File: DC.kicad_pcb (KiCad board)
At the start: 4 copper layers, 125 x 125 mm, 38 parts, among them U6 MCP2551-I-P, U7 NUCLEO-F302R8

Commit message: Imported footprints
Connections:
- U6 pad 8: GND -> Net-(U6-Rs)
- U7 pad CN10_1: unconnected-(U7B-PC9-PadCN10_1) -> /I2C1_SDA
- U7 pad CN10_22: /SupBattMonitor -> unconnected-(U7B-PB2-PadCN10_22)
- U7 pad CN10_23: /AccelIn -> unconnected-(U7B-PA8-PadCN10_23)
- U7 pad CN10_3: unconnected-(U7B-PB8-PadCN10_3) -> /I2C1_CLK
- U7 pad CN7_28: unconnected-(U7A-PA0-PadCN7_28) -> /AccelIn

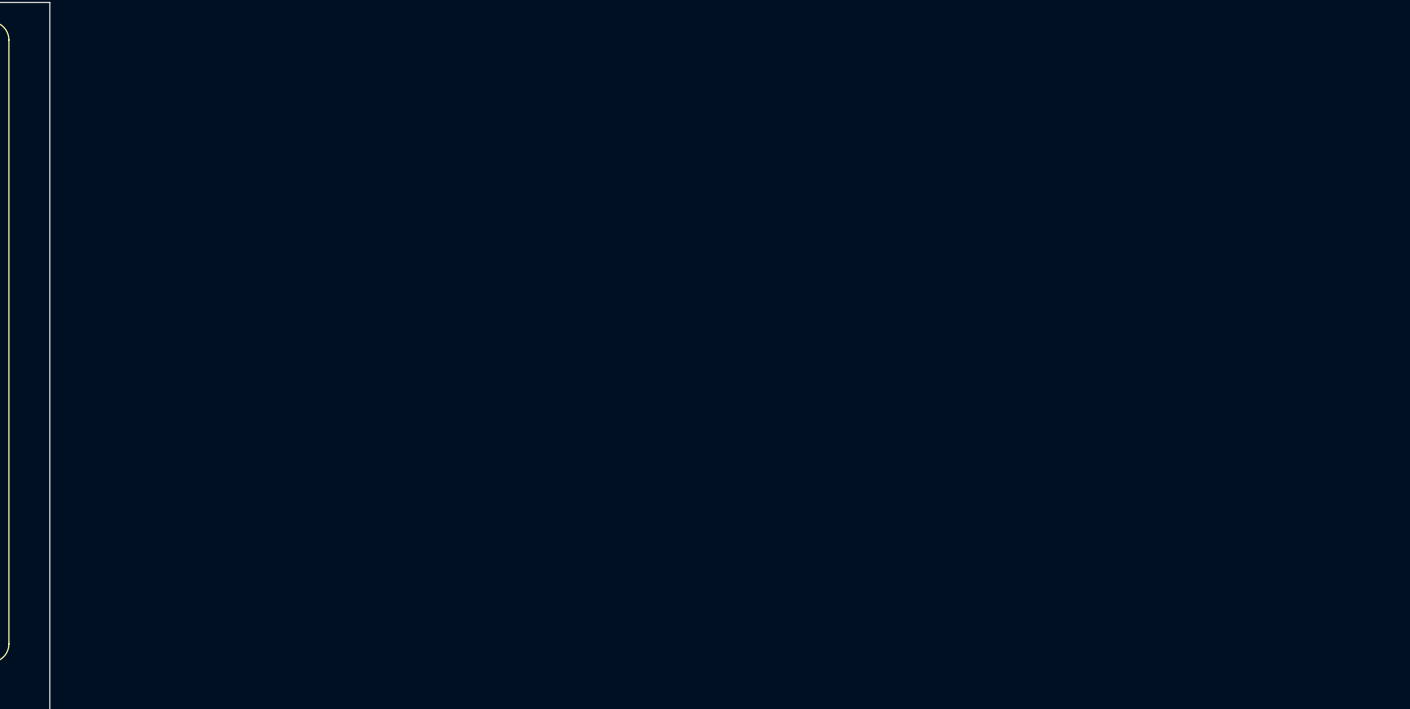
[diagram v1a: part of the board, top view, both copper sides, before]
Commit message: Added LCD!
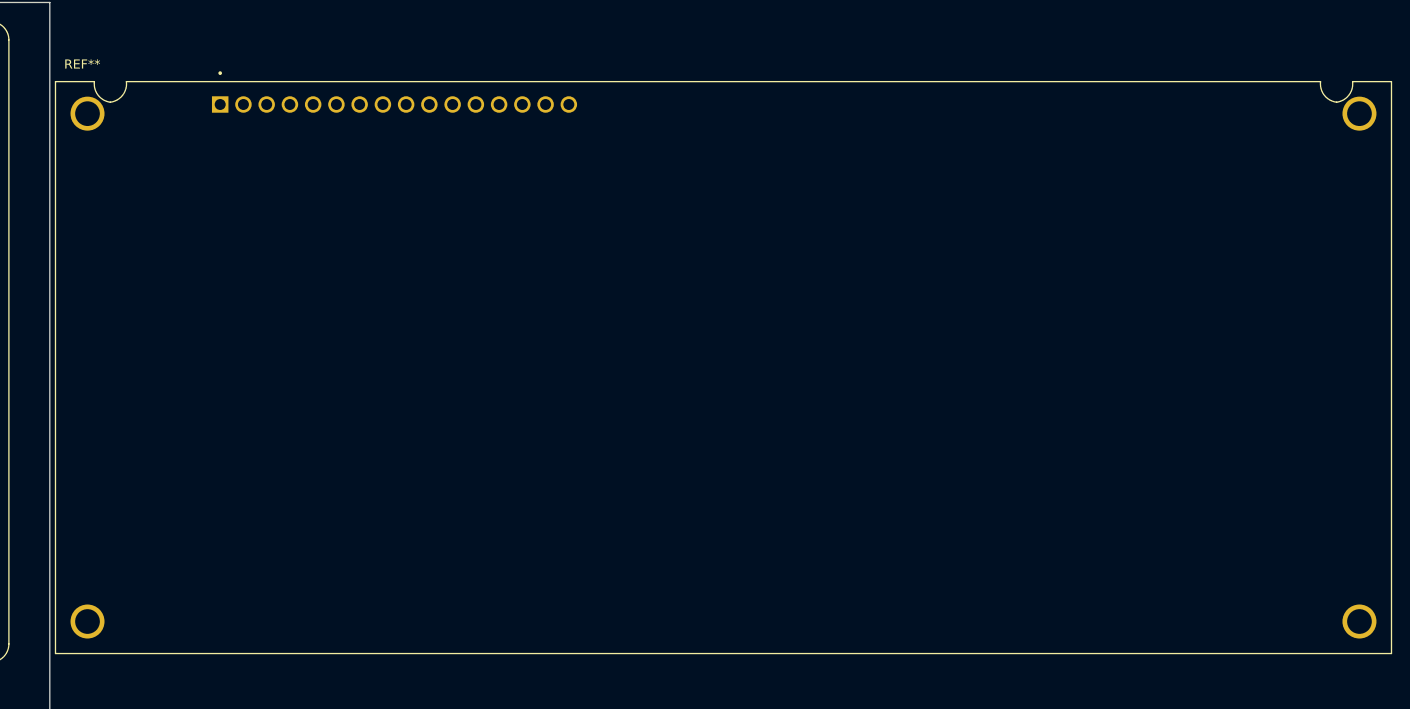
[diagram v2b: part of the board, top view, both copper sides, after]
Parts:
- added REF**: LCD_NHD-0420E2Z-FSW-GBW, MiscellaneousLibrary:LCD_NHD-0420E2Z-FSW-GBW, F.Cu at (256.5, 79.0)

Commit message: Symbols all have a footprint and LCD added
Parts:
- removed REF**: LCD_NHD-0420E2Z-FSW-GBW, MiscellaneousLibrary:LCD_NHD-0420E2Z-FSW-GBW
- added C10: CL31B225KBHNNNE, Capacitor_SMD:CAPC3216X180N, F.Cu at (159.5, 38.5)
- added C11: CL31B105KAHNNNE, Capacitor_SMD:CAPC3216X180N, F.Cu at (167.0, 86.5)
- added C12: C3216X7R2A474K160AA, Capacitor_SMD:CAPC3216X180N, F.Cu at (172.5, 86.5)
- added C8: CL31B225KBHNNNE, Capacitor_SMD:CAPC3216X180N, F.Cu at (161.5, 103.5)
- added C9: CL31B225KBHNNNE, Capacitor_SMD:CAPC3216X180N, F.Cu at (131.5, 103.5)
- added D1: LTST-C190KSKT, LED_SMD:LEDM1608X80, F.Cu at (144.1, 247.6)
- added D2: LTST-C193TBKT-5A, Fuse:Fuse_0603_1608Metric, F.Cu at (138.7, 192.1)
- added D4: LTST-C193TBKT-5A, Fuse:Fuse_0603_1608Metric, F.Cu at (138.7, 194.6)
- added D5: LTST-C193TBKT-5A, Fuse:Fuse_0603_1608Metric, F.Cu at (138.7, 197.1)
- added D6: LTST-C193TBKT-5A, Fuse:Fuse_0603_1608Metric, F.Cu at (138.7, 199.6)
- added D7: LTST-C193TBKT-5A, Fuse:Fuse_0603_1608Metric, F.Cu at (138.7, 202.1)
- added DS1: NHD-C0220BIZ-FSW-FBW-3V3M, Display:LCD_NHD-C0220BIZ-FSW-FBW-3V3M, F.Cu at (174.5, 62.6)
- added F10: 0466.125NR, Fuse:FUSC3215X66N, F.Cu at (133.5, 186.1)
- added F11: 0466.125NR, Fuse:FUSC3215X66N, F.Cu at (138.6, 178.1)
- added F12: 0466.125NR, Fuse:FUSC3215X66N, F.Cu at (138.6, 180.8)
- added F13: 0466.125NR, Fuse:FUSC3215X66N, F.Cu at (138.6, 183.5)
- added F14: 0466.125NR, Fuse:FUSC3215X66N, F.Cu at (138.6, 186.1)
- added F15: 0466.125NR, Fuse:FUSC3215X66N, F.Cu at (143.6, 178.1)
- added F16: 0466.125NR, Fuse:FUSC3215X66N, F.Cu at (143.6, 180.8)
- added F17: 0466.125NR, Fuse:FUSC3215X66N, F.Cu at (143.6, 183.5)
- added F18: 0466.125NR, Fuse:FUSC3215X66N, F.Cu at (143.6, 186.1)
- added F7: 0466.125NR, Fuse:FUSC3215X66N, F.Cu at (133.5, 178.1)
- added F8: 0466.125NR, Fuse:FUSC3215X66N, F.Cu at (133.5, 180.8)
- added F9: 0466.125NR, Fuse:FUSC3215X66N, F.Cu at (133.5, 183.5)
- added J1: 348302001, Connector_Molex:CONN_SD-34829-001_20_ST_MOL, F.Cu at (221.5, 199.5)
- added J2: 348302001, Connector_Molex:CONN_SD-34829-001_20_ST_MOL, F.Cu at (333.5, 198.0)
- added J3: 757570141, Connector_Molex:CONN_SD-75757-010_1X4_F11p20_MOL, F.Cu at (164.0, 146.5)
- added LED1: LTST-C170GKT, LED_SMD:LED_LTST-C170GKT_LTO, F.Cu at (177.0, 114.2)
- added LED2: LTST-C170GKT, LED_SMD:LED_LTST-C170GKT_LTO, F.Cu at (190.5, 115.0)
- added LED3: LTST-C170GKT, LED_SMD:LED_LTST-C170GKT_LTO, F.Cu at (177.0, 120.0)
- added LED4: LTST-C170GKT, LED_SMD:LED_LTST-C170GKT_LTO, F.Cu at (177.0, 122.9)
- added LED5: LTST-C170GKT, LED_SMD:LED_LTST-C170GKT_LTO, F.Cu at (177.0, 125.8)
- added R13: RMCF1206FT4K70, Resistor_SMD:RESC3216X70N, F.Cu at (179.0, 86.5)
- added R15: RC1206FR-0710KL, Resistor_SMD:RESC3116X65N, F.Cu at (160.5, 33.5)
- added R16: RC1206FR-0710KL, Resistor_SMD:RESC3116X65N, F.Cu at (161.5, 98.5)
- added R17: RC1206FR-0710KL, Resistor_SMD:RESC3116X65N, F.Cu at (131.5, 98.5)
- added R18: RC1206FR-07665RL, Resistor_SMD:RESC3116X65N, F.Cu at (133.8, 171.9)
- added R19: RC1206FR-071K24L, Resistor_SMD:RESC3116X65N, F.Cu at (133.8, 175.2)
- added R20: RC1206FR-072K32L, Resistor_SMD:RESC3116X65N, F.Cu at (139.2, 162.0)
- added R21: RC1206FR-102K2L, Resistor_SMD:RESC3116X65N, F.Cu at (139.2, 165.3)
- added R22: RC1206FR-072K32L, Resistor_SMD:RESC3116X65N, F.Cu at (139.2, 168.6)
- added R23: RC1206FR-072K32L, Resistor_SMD:RESC3116X65N, F.Cu at (139.2, 171.9)
- added R24: RC1206FR-072K32L, Resistor_SMD:RESC3116X65N, F.Cu at (139.2, 175.2)
- added R25: RC1206FR-072K32L, Resistor_SMD:RESC3116X65N, F.Cu at (144.7, 162.0)
- added R26: RC1206FR-071K24L, Resistor_SMD:RESC3116X65N, F.Cu at (144.7, 165.3)
- added R27: RC1206FR-071K24L, Resistor_SMD:RESC3116X65N, F.Cu at (144.7, 168.6)
- added R28: RC1206FR-071K24L, Resistor_SMD:RESC3116X65N, F.Cu at (144.7, 171.9)
- added R29: RC1206FR-071K24L, Resistor_SMD:RESC3116X65N, F.Cu at (144.7, 175.2)
- added S1: LP6OA2ASRG, Button_Switch_SMD:LP6OA2ASRG, F.Cu at (167.5, 33.5)
- added S2: LP6OA2ASRG, Button_Switch_SMD:LP6OA2ASRG, F.Cu at (168.8, 98.5)
- added S3: LP6OA2ASRG, Button_Switch_SMD:LP6OA2ASRG, F.Cu at (138.3, 98.5)
- added S4: LP6OA2ASRG, Button_Switch_SMD:LP6OA2ASRG, F.Cu at (114.3, 62.0)
- moved F5 72.5 mm to (79.7, 136.6)
- moved R1 72.5 mm to (72.1, 106.1)
- moved R2 72.5 mm to (64.5, 106.1)
- moved U1 72.5 mm to (72.1, 118.8)
- moved U2 72.5 mm to (64.5, 118.8)
- moved a1 72.5 mm to (-1.34, 129.2)
- moved a2 72.5 mm to (-1.34, 37.5)
- moved a3 72.5 mm to (-1.34, 98.5)
- moved C1 72.5 mm to (20.0, 106.1)
- moved C2 72.5 mm to (20.0, 90.8)
- moved C3 72.5 mm to (20.0, 75.6)
- moved C4 72.5 mm to (20.0, 60.4)
- moved C5 72.5 mm to (20.0, 29.9)
- moved C6 72.5 mm to (20.0, 45.1)
- moved C7 72.5 mm to (31.5, 121.3)
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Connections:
- U7 pad CN10_21: /BrakePedal -> /BrakePedalIn
- U7 pad CN10_24: /RSignalLightButton -> /RSignalLightIn
- U7 pad CN10_25: /LSignalLightButton -> /LSignalLightIn
- U7 pad CN7_38: /HazardButton -> /HazardIn
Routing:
- net GND: track 0.00 -> 33.7 mm, vias 0 -> 3
- net Net-(DS1A-SCL): track 0.00 -> 17.6 mm
- net +3.3V: track 0.00 -> 16.3 mm, vias 0 -> 4
- net /RSignalLightIn: track 0.00 -> 12.0 mm
- net /LSignalLightIn: track 0.00 -> 11.5 mm
- net /HazardIn: track 0.00 -> 10.0 mm
- net Net-(DS1A-C1N): track 0.00 -> 8.80 mm
- net Net-(DS1A-C1P): track 0.00 -> 8.41 mm
- net Net-(DS1A-VOUT): track 0.00 -> 8.19 mm

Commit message: LEDs routed
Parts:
- added C7: C, DriverControlsLib:CAP-TH_L6.0-W3.5-P7.50-D1.0, F.Cu at (154.5, 142.0)
- added D3: LTW-C191DS5, LED_SMD:LEDC1608X65N, F.Cu at (147.0, 105.0)
- added D8: LTST-C190KSKT, LED_SMD:LEDM1608X80, F.Cu at (147.0, 95.0)
- added D9: LTST-C190KSKT, LED_SMD:LEDM1608X80, F.Cu at (147.0, 92.5)
- added F19: 0466.125NR, Fuse:FUSC3215X66N, F.Cu at (157.0, 95.0)
- added F20: 0466.125NR, Fuse:FUSC3215X66N, F.Cu at (157.0, 92.5)
- added J4: PPTC021LFBN-RC, Connector:CONN2_LFBN-RC_SUL, F.Cu at (135.0, 150.0)
- added R10: RC1206FR-0710KL, Resistor_SMD:RESC3116X65N, F.Cu at (199.5, 105.5)
- added R12: 120Ω, DriverControlsLib:RES-TH_BD2.2-L6.5-P10.50-D0.6, F.Cu at (121.5, 129.0)
- added R12: 120Ω, Resistor_SMD:RESC3116X65N, F.Cu at (162.0, 111.0)
- added R14: 120Ω, DriverControlsLib:RES-TH_BD2.2-L6.5-P10.50-D0.6, F.Cu at (135.0, 139.0)
- added R6: RC1206FR-07665RL, Resistor_SMD:RESC3116X65N, F.Cu at (152.0, 95.0)
- added R7: RC1206FR-07665RL, Resistor_SMD:RESC3116X65N, F.Cu at (152.0, 92.5)
- added R8: RC1206FR-0710KL, Resistor_SMD:RESC3116X65N, F.Cu at (162.5, 125.5)
- added R9: RC1206FR-0710KL, Resistor_SMD:RESC3116X65N, F.Cu at (199.5, 102.2)
- added S5: 100SP1T8B13VS2REH, Button_Switch_SMD:100SP1T8B13VS2REH, F.Cu at (99.5, 113.3)
- added U6: MCP2551-I-P, Package_DIP:DIP-8_W7.62mm, F.Cu at (149.4, 145.8)
- added U7: NUCLEO-F302R8, DriverControlsLib:MODULE_NUCLEO-F302R8, F.Cu at (254.4, 52.9)
- moved D1 150.2 mm to (147.0, 97.5)
- moved D2 137.6 mm to (103.5, 59.0), turned to 180 degrees
- moved D4 135.7 mm to (103.5, 63.5), turned to 180 degrees
- moved D5 133.7 mm to (103.7, 68.0), turned to 180 degrees
- moved D6 131.8 mm to (103.7, 72.5), turned to 180 degrees
- moved F9 131.1 mm to (92.5, 59.0)
- moved D7 129.9 mm to (103.7, 77.0), turned to 180 degrees
- moved F11 123.5 mm to (92.5, 63.5)
- moved F12 121.8 mm to (92.5, 68.0)
- moved F13 120.2 mm to (92.5, 72.5)
- moved F14 118.5 mm to (92.5, 77.0)
- moved J2 116.8 mm to (221.5, 165.0)
- moved F18 115.0 mm to (203.5, 88.0)
- moved R22 112.7 mm to (98.5, 63.5)
- moved R23 111.6 mm to (98.5, 68.0)
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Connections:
- C12 pad 2: +3.3V -> GND
- DS1 pad 1: /RST -> Net-(DS1A-RST)
- DS1 pad 2: Net-(DS1A-SCL) -> /I2C1_CLK
- DS1 pad 3: Net-(DS1A-SCL) -> /I2C1_SDA
- DS1 pad A: (no net) -> +3.3V
- DS1 pad K: (no net) -> GND
- F10 pad 1: +12V -> /DashFaultIndicator
- F11 pad 1: +12V -> /BlueLED2
- F12 pad 1: +12V -> /BlueLED3
- F13 pad 1: +12V -> /BlueLED4
- F14 pad 1: +12V -> /BlueLED5
- F15 pad 1: +12V -> /GreenLED2
- F16 pad 1: +12V -> /GreenLED3
- F17 pad 1: +12V -> /GreenLED4
- F18 pad 1: +12V -> /GreenLED5
- F7 pad 1: +12V -> /HVILActive
- F8 pad 1: +12V -> /GreenLED1
- F9 pad 1: +12V -> /BlueLED1
- J2 pad 10: /BrakeLight3 -> /BrakeLightNeg
- J2 pad 11: /DRLLeft -> /DRLLeftNeg
- J2 pad 12: /DRLRight -> /DRLRightNeg
- J2 pad 13: /LSignalLight1 -> /LSignalLightNeg
- J2 pad 14: /LSignalLight2 -> /LSignalLightNeg
- J2 pad 15: /LSignalLight3 -> /LSignalLightNeg
- J2 pad 16: /RSignalLight1 -> /RSignalLightNeg
- J2 pad 17: /RSignalLight2 -> /RSignalLightNeg
- J2 pad 18: /RSignalLight3 -> /RSignalLightNeg
- J2 pad 19: unconnected-(J2-Pad19) -> /ThermalShutoff
- J2 pad 8: /BrakeLight1 -> /BrakeLightNeg
- J2 pad 9: /BrakeLight2 -> /BrakeLightNeg
- R14 pad 1: /CAN_H -> Net-(J4-Pad2)
- S4 pad 1: +3.3V -> /To_PreChargeBtn
- S4 pad 2: unconnected-(S4-Pad2) -> /From_PreChargeBtn
- S4 pad 3: /To_PreChargeBtn -> unconnected-(S4-Pad3)
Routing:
- net Net-(DS1A-SCL): track 17.6 -> 0.00 mm
- net /CANTransceiver5V: track 145.3 -> 155.4 mm
- net /CAN_L: track 57.6 -> 67.4 mm
- net /CAN_H: track 57.5 -> 67.1 mm
- net GND: track 33.7 -> 43.1 mm, vias 3 -> 7
- net Net-(DS1A-C1N): track 8.80 -> 0.50 mm
- net +3.3V: track 16.3 -> 8.10 mm, vias 4 -> 3
- net Net-(DS1A-C1P): track 8.41 -> 0.50 mm
- net Net-(DS1A-VOUT): track 8.19 -> 0.50 mm
- net /CAN_RX: track 53.9 -> 60.9 mm
- net /CAN_TX: track 71.2 -> 76.3 mm
- net Net-(F9-Pad2): track 0.00 -> 3.08 mm
- net Net-(F14-Pad2): track 0.00 -> 3.06 mm
- net Net-(F13-Pad2): track 0.00 -> 3.06 mm
- net Net-(F12-Pad2): track 0.00 -> 3.06 mm
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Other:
- board size 125 x 125 mm -> 237.5 x 213.5 mm

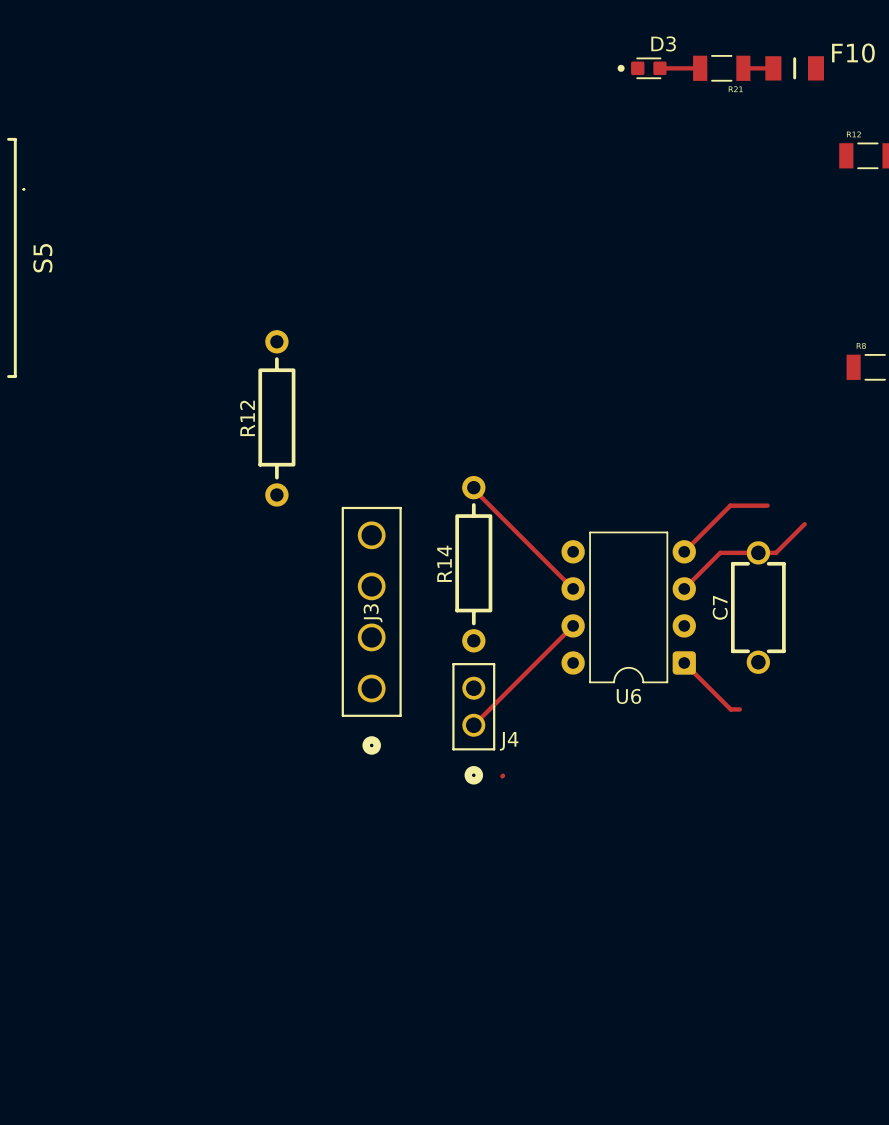
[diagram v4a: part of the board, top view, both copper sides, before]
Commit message: Added HV and LV switches
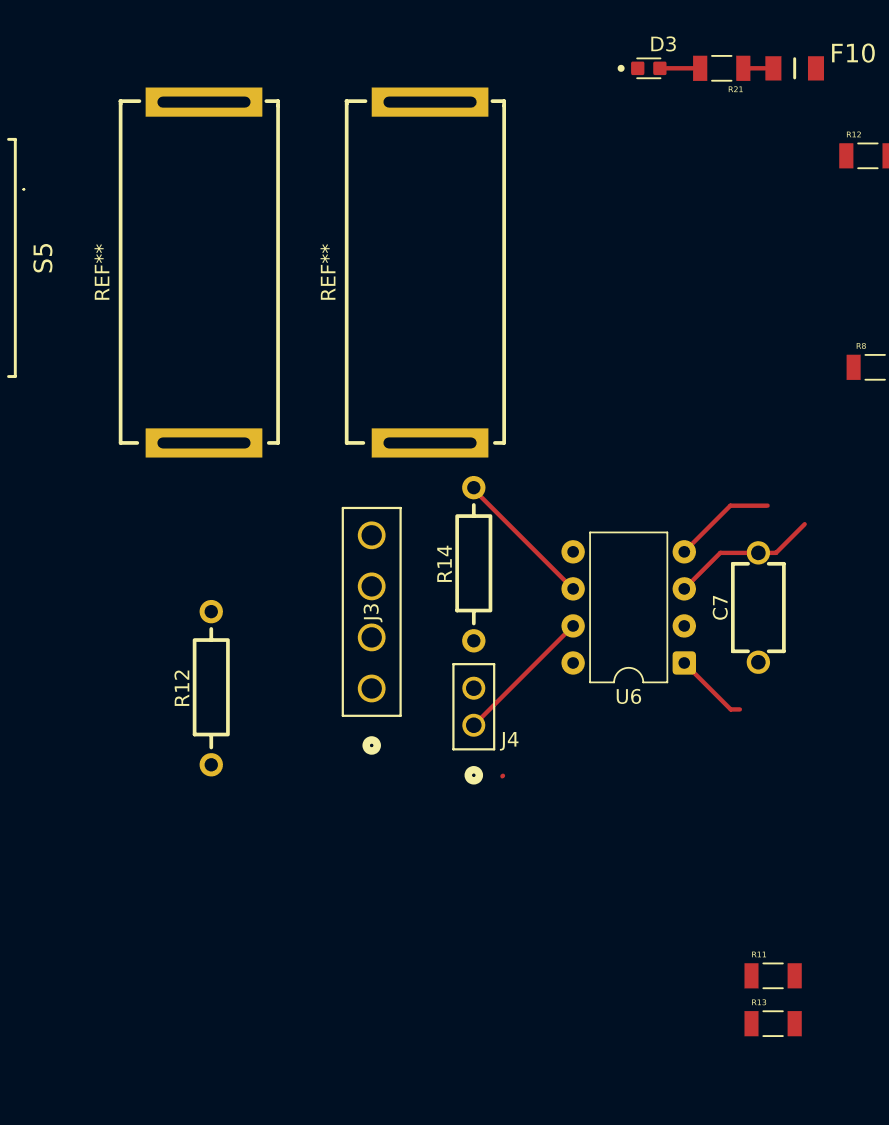
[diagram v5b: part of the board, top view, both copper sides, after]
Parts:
- added R11: RC1206JR-07120RL, Resistor_SMD:RESC3116X65N, F.Cu at (155.5, 167.2)
- added R13: RC1206JR-07120RL, Resistor_SMD:RESC3116X65N, F.Cu at (155.5, 170.5)
- added REF**: LVSwitch, LV_Switch:New footprint 1, F.Cu at (132.0, 119.0)
- added REF**: HVSwitch, HV_Switch:New footprint 1, F.Cu at (116.5, 119.0)
- moved R12 19.0 mm to (117.0, 147.5)
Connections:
- J4 pad 2: /CAN_L -> Net-(J4-Pad2)

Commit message: Routed front and back
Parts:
- removed C1, C2, C3, C4, C5, C6: C, DriverControlsLib:CAP-TH_L6.0-W3.5-P7.50-D1.0
- removed the C7 at (-27.5, 107.8)
- removed F6: ~, DriverControlsLib:FUSE-TH_BD5.4-W22.5-P27.5-D0.8
- removed the R10 at (-45.3, 16.4)
- removed the R11 at (-45.3, 31.6)
- removed R12, R14 (x2): 120Ω, DriverControlsLib:RES-TH_BD2.2-L6.5-P10.50-D0.6
- removed R12: 12kΩ, DriverControlsLib:RES-TH_BD2.2-L6.5-P10.50-D0.6
- removed R12: 120Ω, Resistor_SMD:RESC3116X65N
- removed the R13 at (154.5, 78.7)
- removed the R13 at (-27.5, 92.6)
- removed the R6 at (-45.3, 92.6)
- removed the R7 at (-45.3, 77.3)
- removed the R8 at (-45.3, 62.1)
- removed the R9 at (-45.3, 46.9)
- removed the U6 at (149.4, 145.8)
- removed the U6 at (-32.6, 111.6)
- removed the U7 at (8.03, 44.3)
- removed the U7 at (254.4, 52.9)
- removed a1, a2, a3, a4: ~, DriverControlsLib:Molex 8 Pin Mini-fit TPA
- added D10: NUP2105LT1G, Diode_SMD:SOT95P237X111-3N, F.Cu at (112.7, 177.3)
- added U6: MCP2551-I-P, Package_DIP:DIP-8_W7.62mm, F.Cu at (108.4, 162.5)
- added U7: NUCLEO-F302R8, Module:MODULE_NUCLEO-F302R8, F.Cu at (116.2, 98.8)
- F1, F2, F3, F4, F5: footprint DriverControlsLib:FUSE-TH_BD5.4-W22.5-P27.5-D0.8 -> Fuse:FUSC3215X66N
- R1, R2, R3, R4, R5: footprint DriverControlsLib:RES-TH_BD2.2-L6.5-P10.50-D0.6 -> Resistor_SMD:RESC3216X70N
- U1, U2, U3, U4, U5: footprint DriverControlsLib:TO220-3_ONS -> Battery:TO254P470X1016X2019-3P
- moved C8 158.1 mm to (262.8, 35.0), turned to 180 degrees
- moved R16 154.6 mm to (262.8, 40.0), turned to 180 degrees
- moved S2 141.0 mm to (255.5, 40.0), turned to 180 degrees
- moved S4 139.3 mm to (216.2, 104.5)
- moved F3 131.7 mm to (90.5, 162.5), turned to 180 degrees
- moved R3 123.1 mm to (84.0, 162.4), turned to 0 degrees
- moved S5 122.9 mm to (213.5, 67.3)
- moved R4 121.9 mm to (84.0, 170.5), turned to 0 degrees
- moved R5 121.9 mm to (84.0, 178.8), turned to 0 degrees
- moved U3 119.2 mm to (84.6, 167.1), turned to 0 degrees
- moved U4 117.8 mm to (84.9, 175.4), turned to 0 degrees
- moved U5 117.2 mm to (84.9, 183.8), turned to 0 degrees
- moved J1 116.4 mm to (247.5, 181.5)
- moved D2 112.0 mm to (208.5, 98.0)
- moved D4 112.0 mm to (208.5, 102.5)
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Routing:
- net /HVActive: track 0.00 -> 322.4 mm
- net /LVActive: track 0.00 -> 310.5 mm, vias 0 -> 4
- net /DashFaultIndicator: track 0.00 -> 300.8 mm, vias 0 -> 2
- net /HVILActive: track 0.00 -> 300.8 mm, vias 0 -> 4
- net /LVSwitch+: track 0.00 -> 234.3 mm, vias 0 -> 3
- net /RSignalLightIn: track 12.0 -> 245.8 mm, vias 0 -> 4
- net /LVSwitch-: track 0.00 -> 205.3 mm, vias 0 -> 3
- net /HVSwitch-: track 0.00 -> 189.5 mm, vias 0 -> 2
- net VCC: track 176.4 -> 0.00 mm
- net /From_PreChargeBtn: track 0.00 -> 176.3 mm
- net /To_PreChargeBtn: track 0.00 -> 169.5 mm
- net /HVSwitch+: track 0.00 -> 166.6 mm, vias 0 -> 6
- net /BlueLED1: track 0.00 -> 158.4 mm
- net /BlueLED2: track 0.00 -> 151.1 mm
- net /To_ModeSelect: track 0.00 -> 142.5 mm, vias 0 -> 1
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- added copper zone on In1.Cu, net (none)
- removed copper zone on In1.Cu, net /+3V3
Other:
- board size 237.5 x 213.5 mm -> 196.5 x 181.5 mm
- board text removed: "1"
- board text removed: "2"
- board text removed: "3"
- board text removed: "4"
- board text removed: "5"
- board text removed: "6"
- board text removed: "7"
- board text removed: "8"
- board text removed: "CAN VCC Gear"
- board text removed: "CANH"
- board text removed: "CANL"
- board text removed: "Extra Pins"
- board text removed: "Lights"
- board text removed: "VCC"
- board text removed: "to Buttons"
- board text removed: "~"
